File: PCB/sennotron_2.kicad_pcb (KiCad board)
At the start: 2 copper layers, 30 parts, among them J1 Barrel_Jack, J2 Raspberry_Pi_2_3, J3 Conn_02x08_Odd_Even, J4 Conn_01x16_Female, J5 Screw_Terminal_01x04, J6 Screw_Terminal_01x16, J7 Conn_02x04_Odd_Even, J9 Conn_01x05_Female, U1 LM1117-3.3, U2 MCP3208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

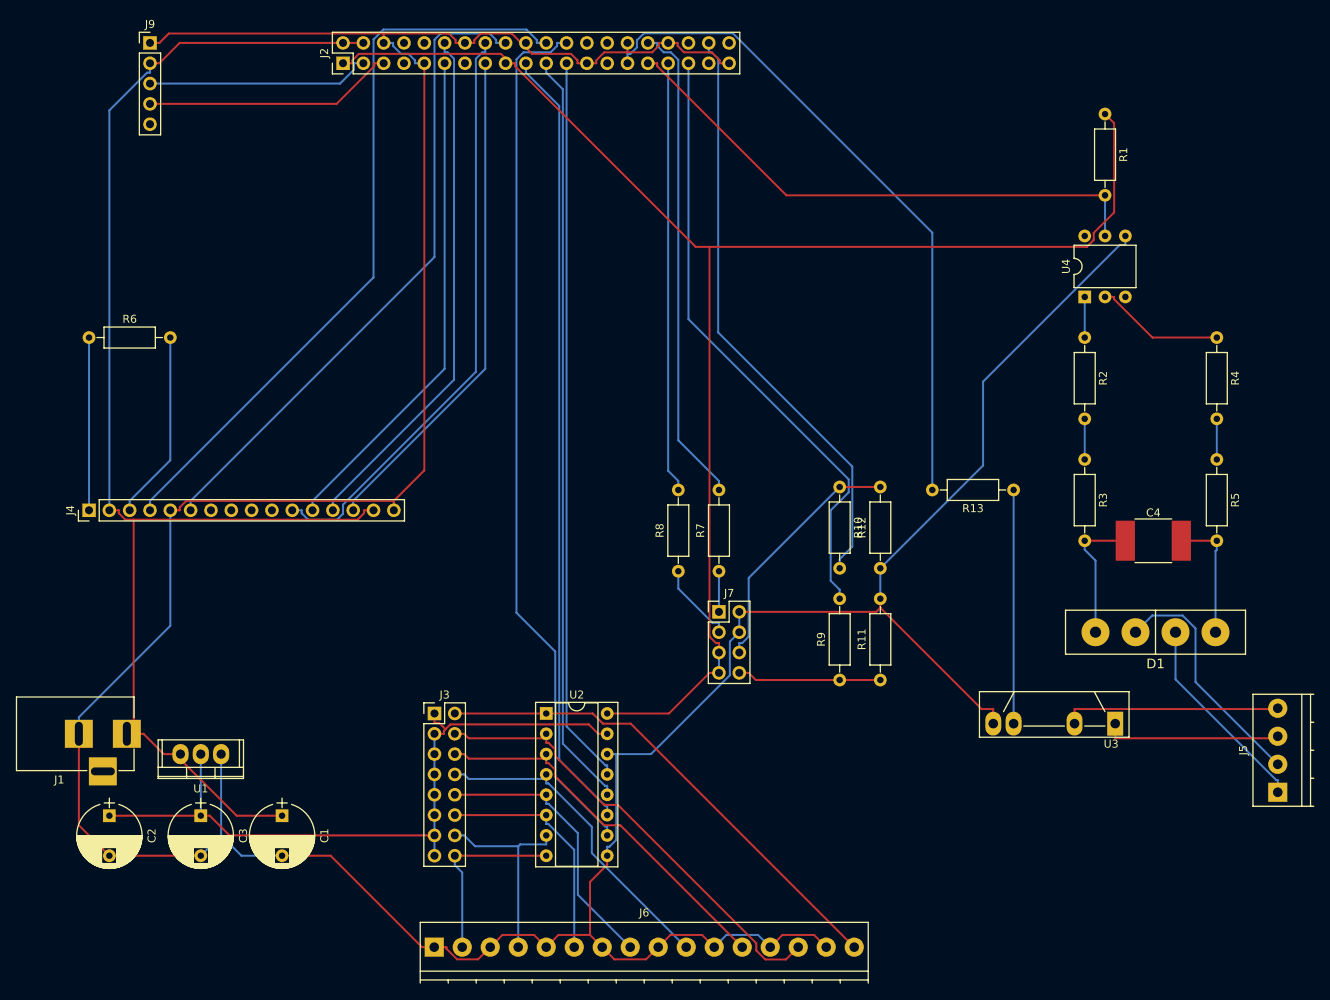
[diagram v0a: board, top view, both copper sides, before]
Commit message: ...
Redesigned the pcb. Some Additions in the .sch. Moved the new pcb to "_2"
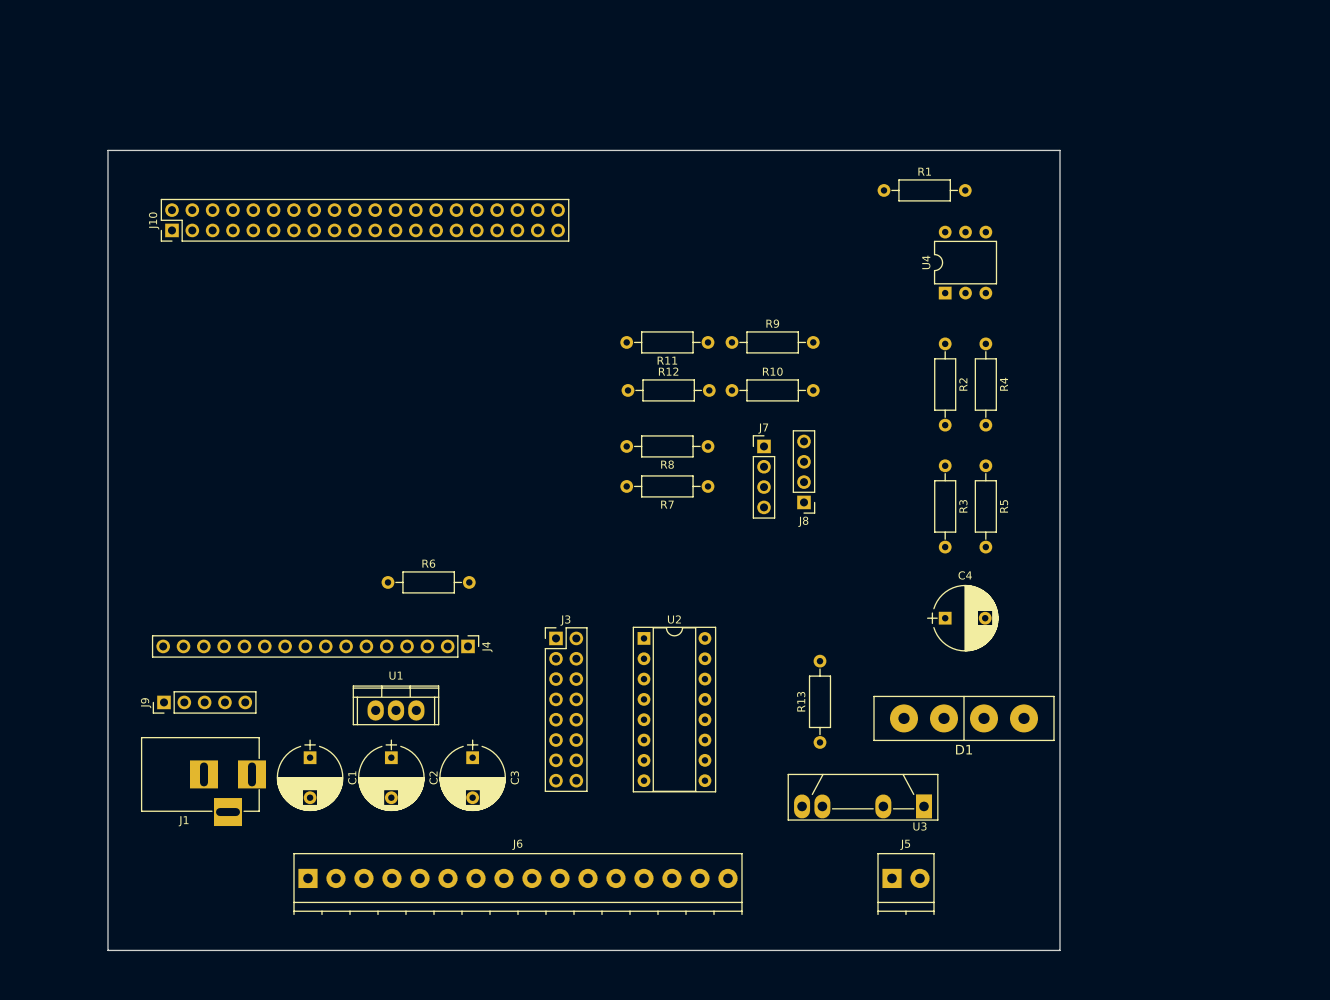
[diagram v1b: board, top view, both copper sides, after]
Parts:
- removed J2: Raspberry_Pi_2_3, Pin_Headers:Pin_Header_Straight_2x20_Pitch2.54mm
- added J10: Conn_02x20_Odd_Even, Pin_Headers:Pin_Header_Straight_2x20_Pitch2.54mm, F.Cu at (98.0, 59.0)
- added J8: Conn_01x04_Male, Pin_Headers:Pin_Header_Straight_1x04_Pitch2.54mm, F.Cu at (177.0, 93.0)
- C4: footprint Capacitors_SMD:C_2220_HandSoldering -> Capacitors_THT:CP_Radial_D8.0mm_P5.00mm
- D1: value D_Bridge_+AA- -> D_Bridge_+-AA
- J5: value Screw_Terminal_01x04 -> Screw_Terminal_01x02; footprint TerminalBlocks_Phoenix:TerminalBlock_Phoenix_PT-3.5mm_4pol -> TerminalBlocks_Phoenix:TerminalBlock_Phoenix_PT-3.5mm_2pol
- J7: value Conn_02x04_Odd_Even -> Conn_01x04_Male; footprint Pin_Headers:Pin_Header_Straight_2x04_Pitch2.54mm -> Pin_Headers:Pin_Header_Straight_1x04_Pitch2.54mm
- moved J9 82.5 mm to (97.0, 118.0), turned to 90 degrees
- moved J4 50.3 mm to (135.0, 111.0), turned to 270 degrees
- moved J5 49.4 mm to (188.0, 140.0), turned to 0 degrees
- moved R6 48.3 mm to (125.0, 103.0)
- moved R11 47.4 mm to (165.0, 73.0), turned to 180 degrees
- moved R9 44.3 mm to (168.0, 73.0), turned to 0 degrees
- moved R13 39.8 mm to (179.0, 123.0), turned to 90 degrees
- moved R12 38.6 mm to (155.0, 79.0), turned to 0 degrees
- moved C2 36.0 mm to (125.4, 124.9)
- moved C3 34.7 mm to (135.6, 124.9)
- moved R1 29.2 mm to (187.0, 54.0), turned to 0 degrees
- moved R4 28.9 mm to (199.7, 73.2)
- moved R5 28.9 mm to (199.7, 88.4)
- moved C4 27.8 mm to (194.7, 107.5)
- moved D1 26.3 mm to (197.0, 120.0)
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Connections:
- D1 pad 2: Net-(D1-Pad2) -> Net-(C4-Pad2)
- D1 pad 3: Net-(D1-Pad3) -> /220L
- D1 pad 4: Net-(C4-Pad2) -> Net-(D1-Pad4)
- J1 pad 3: Net-(J1-Pad3) -> (no net)
- J4 pad 1: Net-(J4-Pad1) -> GND
- J4 pad 10: Net-(J4-Pad10) -> (no net)
- J4 pad 11: lcd_d4 -> /lcd3
- J4 pad 12: lcd_d5 -> /lcd4
- J4 pad 13: lcd_d6 -> /lcd5
- J4 pad 14: lcd_d7 -> /lcd6
- J4 pad 4: lcd_rs -> /lcd1
- J4 pad 6: lcd_en -> /lcd2
- J4 pad 7: Net-(J4-Pad7) -> (no net)
- J4 pad 8: Net-(J4-Pad8) -> (no net)
- J4 pad 9: Net-(J4-Pad9) -> (no net)
- J5 pad 1: Net-(D1-Pad3) -> Net-(D1-Pad4)
- J5 pad 2: Net-(D1-Pad2) -> /220L
- J6 pad 1: GND -> Net-(J3-Pad2)
- J6 pad 10: Net-(J3-Pad8) -> GND
- J6 pad 11: GND -> Net-(J3-Pad12)
- J6 pad 12: Net-(J3-Pad6) -> GND
- J6 pad 13: GND -> Net-(J3-Pad14)
- J6 pad 14: Net-(J3-Pad4) -> GND
- J6 pad 15: GND -> Net-(J3-Pad16)
- J6 pad 16: Net-(J3-Pad2) -> GND
- J6 pad 2: Net-(J3-Pad16) -> GND
- J6 pad 3: GND -> Net-(J3-Pad4)
- J6 pad 4: Net-(J3-Pad14) -> GND
- J6 pad 5: GND -> Net-(J3-Pad6)
- J6 pad 6: Net-(J3-Pad12) -> GND
- J6 pad 7: GND -> Net-(J3-Pad8)
- J6 pad 8: Net-(J3-Pad10) -> GND
- J6 pad 9: GND -> Net-(J3-Pad10)
- J7 pad 3: Net-(J7-Pad3) -> GND
- J7 pad 4: GND -> Net-(J7-Pad4)
- J9 pad 5: Net-(J9-Pad5) -> (no net)
- R10 pad 1: Net-(J7-Pad6) -> Net-(J8-Pad1)
- R10 pad 2: btn_2 -> /btn2
- R11 pad 1: Net-(J7-Pad8) -> Net-(J8-Pad4)
- R12 pad 2: Net-(J7-Pad6) -> Net-(J8-Pad1)
- R6 pad 1: Net-(J4-Pad1) -> GND
- R7 pad 1: Net-(J7-Pad1) -> Net-(J7-Pad4)
- R7 pad 2: led_1 -> /led1
- R8 pad 1: Net-(J7-Pad3) -> Net-(J7-Pad1)
- R8 pad 2: led_2 -> /led2
- R9 pad 1: Net-(J7-Pad8) -> Net-(J8-Pad4)
- R9 pad 2: btn_1 -> /btn1
- U3 pad 1: Net-(J5-Pad3) -> Net-(D1-Pad4)
- U3 pad 2: Net-(J5-Pad4) -> /220L
- U4 pad 3: Net-(U4-Pad3) -> (no net)
- U4 pad 6: Net-(U4-Pad6) -> (no net)
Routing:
- net GND: track 490.2 -> 0.00 mm
- net +3V3: track 193.0 -> 0.00 mm
- net +5V: track 171.4 -> 0.00 mm
- net spi_cs_0: track 109.2 -> 0.00 mm
- net spi_mosi: track 98.3 -> 0.00 mm
- net spi_miso: track 94.8 -> 0.00 mm
- net lcd_rs: track 93.4 -> 0.00 mm
- net spi_clk: track 91.1 -> 0.00 mm
- net +3.3VA: track 90.3 -> 0.00 mm
- net heat_trig: track 83.3 -> 0.00 mm
- net lcd_en: track 81.4 -> 0.00 mm
- net btn_1: track 76.6 -> 0.00 mm
- net btn_2: track 74.0 -> 0.00 mm
- net lcd_d4: track 73.8 -> 0.00 mm
- net AC_sens: track 69.3 -> 0.00 mm
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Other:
- board outline added: 119 x 100 mm

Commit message: pcb design almost done... waiting for a review!
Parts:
- added J11: Conn_01x01, custom:Pad_2.5, F.Cu at (103.0, 65.5)
- added J12: Conn_01x01, custom:Pad_2.5, F.Cu at (110.5, 65.5)
- added J14: Conn_01x01, custom:Pad_2.5, F.Cu at (133.0, 87.0)
- added J15: Conn_01x01, custom:Pad_2.5, F.Cu at (100.5, 87.0)
- added J16: Conn_01x01, custom:Pad_2.5, F.Cu at (111.0, 113.0)
- added J18: Conn_01x01, custom:Pad_2.5, F.Cu at (95.8, 102.2)
- added J19: Conn_01x01, custom:Pad_2.5, F.Cu at (95.8, 89.2)
- added R14: R, Resistors_THT:R_Axial_DIN0207_L6.3mm_D2.5mm_P10.16mm_Horizontal, F.Cu at (182.0, 121.0)
- added U5: S102S01, Housings_SIP:SIP4_Sharp-SSR_Pitch7.62mm_Straight, F.Cu at (204.0, 121.2)
- J1: value Barrel_Jack -> Screw_Terminal_01x02; footprint Connectors:BARREL_JACK -> TerminalBlocks_Phoenix:TerminalBlock_Phoenix_PT-3.5mm_2pol
- J10: footprint Pin_Headers:Pin_Header_Straight_2x20_Pitch2.54mm -> custom:raspberry_pi_zero
- J4: moved to B.Cu
- J5: value Screw_Terminal_01x02 -> Conn_02x04_Odd_Even; footprint TerminalBlocks_Phoenix:TerminalBlock_Phoenix_PT-3.5mm_2pol -> Pin_Headers:Pin_Header_Straight_2x04_Pitch2.54mm
- J6: footprint TerminalBlocks_Phoenix:TerminalBlock_Phoenix_PT-3.5mm_16pol -> custom:springlock
- J7: value Conn_01x04_Male -> Screw_Terminal_01x04; footprint Pin_Headers:Pin_Header_Straight_1x04_Pitch2.54mm -> TerminalBlocks_Phoenix:TerminalBlock_Phoenix_PT-3.5mm_4pol
- J8: value Conn_01x04_Male -> Conn_01x01; footprint Pin_Headers:Pin_Header_Straight_1x04_Pitch2.54mm -> custom:Pad_2.5
- moved J8 83.4 mm to (96.0, 113.0), turned to 0 degrees
- moved J5 63.4 mm to (157.5, 84.5)
- moved J7 57.1 mm to (190.0, 140.2), turned to 90 degrees
- moved R1 55.7 mm to (171.5, 107.5)
- moved J6 38.7 mm to (153.7, 138.5)
- moved J4 35.1 mm to (101.0, 102.2)
- moved R6 29.6 mm to (95.9, 108.6)
- moved U3 26.8 mm to (211.0, 112.0)
- moved J9 26.2 mm to (101.0, 92.1)
- moved R12 23.1 mm to (174.0, 92.1), turned to 270 degrees
- moved R11 19.4 mm to (168.3, 92.1), turned to 270 degrees
- moved D1 18.5 mm to (203.1, 102.5)
- moved R5 18.2 mm to (206.3, 71.4)
- moved R3 18.2 mm to (201.2, 71.4)
- moved R9 16.5 mm to (168.3, 89.5), turned to 90 degrees
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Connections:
- D1 pad 3: /220L -> Net-(D1-Pad3)
- J10 pad 10: /lcd5 -> lcd_en
- J10 pad 12: /lcd4 -> lcd_d4
- J10 pad 14: (no net) -> Net-(J10-Pad14)
- J10 pad 16: /lcd3 -> lcd_d5
- J10 pad 18: /lcd2 -> lcd_d6
- J10 pad 22: /lcd1 -> lcd_d7
- J10 pad 26: (no net) -> Net-(J10-Pad26)
- J10 pad 27: (no net) -> Net-(J10-Pad27)
- J10 pad 28: (no net) -> Net-(J10-Pad28)
- J10 pad 30: GND -> Net-(J10-Pad30)
- J10 pad 32: (no net) -> Net-(J10-Pad32)
- J10 pad 34: GND -> Net-(J10-Pad34)
- J10 pad 36: (no net) -> Net-(J10-Pad36)
- J10 pad 37: (no net) -> Net-(J10-Pad37)
- J10 pad 38: heat_trig -> AC_sens
- J10 pad 40: AC_sens -> heat_trig
- J10 pad 6: GND -> Net-(J10-Pad6)
- J10 pad 8: /lcd6 -> lcd_rs
- J4 pad 10: (no net) -> Net-(J4-Pad10)
- J4 pad 11: /lcd3 -> lcd_d4
- J4 pad 12: /lcd4 -> lcd_d5
- J4 pad 13: /lcd5 -> lcd_d6
- J4 pad 14: /lcd6 -> lcd_d7
- J4 pad 4: /lcd1 -> lcd_rs
- J4 pad 6: /lcd2 -> lcd_en
- J4 pad 7: (no net) -> Net-(J4-Pad7)
- J4 pad 8: (no net) -> Net-(J4-Pad8)
- J4 pad 9: (no net) -> Net-(J4-Pad9)
- J5 pad 1: Net-(D1-Pad4) -> Net-(J5-Pad1)
- J5 pad 2: /220L -> GND
- J6 pad 1: Net-(J3-Pad2) -> GND
- J6 pad 10: GND -> Net-(J3-Pad8)
- J6 pad 11: Net-(J3-Pad12) -> GND
- J6 pad 12: GND -> Net-(J3-Pad6)
- J6 pad 13: Net-(J3-Pad14) -> GND
- J6 pad 14: GND -> Net-(J3-Pad4)
- J6 pad 15: Net-(J3-Pad16) -> GND
- J6 pad 16: GND -> Net-(J3-Pad2)
- J6 pad 2: GND -> Net-(J3-Pad16)
- J6 pad 3: Net-(J3-Pad4) -> GND
- J6 pad 4: GND -> Net-(J3-Pad14)
- J6 pad 5: Net-(J3-Pad6) -> GND
- J6 pad 6: GND -> Net-(J3-Pad12)
- J6 pad 7: Net-(J3-Pad8) -> GND
- J6 pad 8: GND -> Net-(J3-Pad10)
- J6 pad 9: Net-(J3-Pad10) -> GND
- J7 pad 2: GND -> Net-(D1-Pad4)
- J7 pad 3: GND -> Net-(J7-Pad3)
- J7 pad 4: Net-(J7-Pad4) -> Net-(D1-Pad3)
- J8 pad 1: Net-(J8-Pad1) -> GND
- J9 pad 5: (no net) -> Net-(J9-Pad5)
- R10 pad 1: Net-(J8-Pad1) -> Net-(J5-Pad8)
- R11 pad 1: Net-(J8-Pad4) -> Net-(J5-Pad6)
- R12 pad 1: GND -> Net-(J5-Pad8)
- R12 pad 2: Net-(J8-Pad1) -> GND
- R7 pad 1: Net-(J7-Pad4) -> Net-(J5-Pad1)
- R8 pad 1: Net-(J7-Pad1) -> Net-(J5-Pad3)
- R9 pad 1: Net-(J8-Pad4) -> Net-(J5-Pad6)
- U3 pad 1: Net-(D1-Pad4) -> Net-(J7-Pad1)
- U3 pad 2: /220L -> Net-(D1-Pad4)
- U4 pad 3: (no net) -> Net-(U4-Pad3)
- U4 pad 6: (no net) -> Net-(U4-Pad6)
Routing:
- net GND: track 0.00 -> 513.8 mm, vias 0 -> 4
- net +5V: track 0.00 -> 234.7 mm
- net +3.3VA: track 0.00 -> 134.6 mm
- net +3V3: track 0.00 -> 124.3 mm, vias 0 -> 3
- net AC_sens: track 0.00 -> 121.7 mm
- net spi_cs_0: track 0.00 -> 100.9 mm
- net heat_trig: track 0.00 -> 97.9 mm
- net spi_mosi: track 0.00 -> 93.9 mm
- net spi_miso: track 0.00 -> 90.5 mm
- net spi_clk: track 0.00 -> 86.9 mm
- net Net-(J3-Pad2): track 0.00 -> 72.5 mm, vias 0 -> 2
- net Net-(J3-Pad4): track 0.00 -> 66.5 mm
- net Net-(J3-Pad6): track 0.00 -> 60.2 mm
- net lcd_d7: track 0.00 -> 59.4 mm
- net lcd_d6: track 0.00 -> 55.4 mm
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- added copper zone on B.Cu, net GND
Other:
- board size 119 x 100 mm -> 135.5 x 95.5 mm
- copper layers 2 -> 4
- net class 5v added: clearance 0.2, trace_width 0.75, via_dia 0.6, via_drill 0.4
- net class AC added: clearance 0.5, trace_width 2, via_dia 0.6, via_drill 0.4
- net class Default: trace_width 0.25 -> 0.5
- net class lcd added: clearance 0.2, trace_width 0.75, via_dia 0.6, via_drill 0.4
- rule trace_min: 0.2 -> 0.5
